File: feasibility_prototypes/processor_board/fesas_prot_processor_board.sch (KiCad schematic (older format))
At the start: 21 parts, among them P1 CONN_01X08, P10 CONN_01X02, P2 CONN_01X08, P3 CONN_01X02, P4 CONN_01X06, P5 CONN_01X08, P6 CONN_01X08, P7 CONN_01X08, P8 CONN_01X08, P9 CONN_01X02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

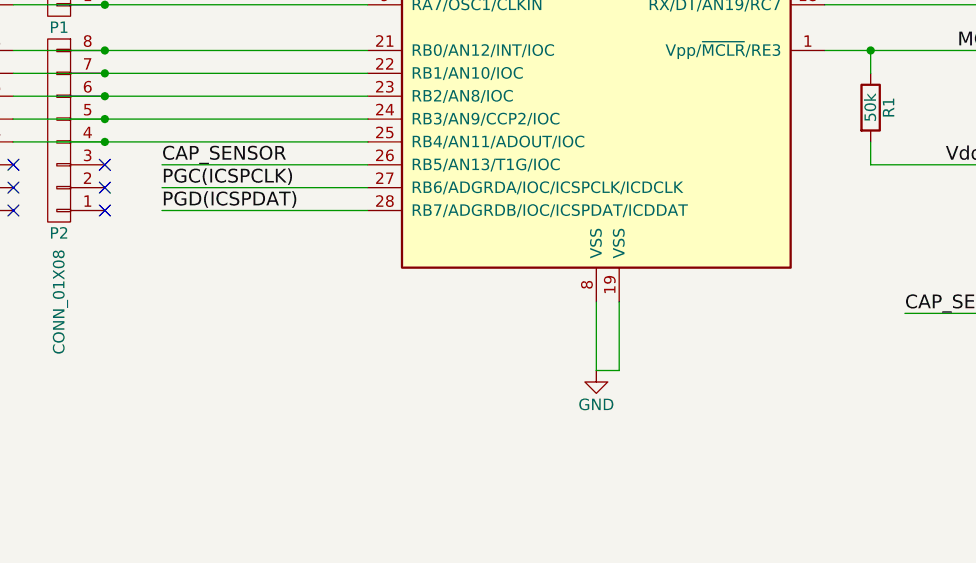
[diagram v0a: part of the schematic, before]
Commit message: Addded guard trace for cap-sense pad
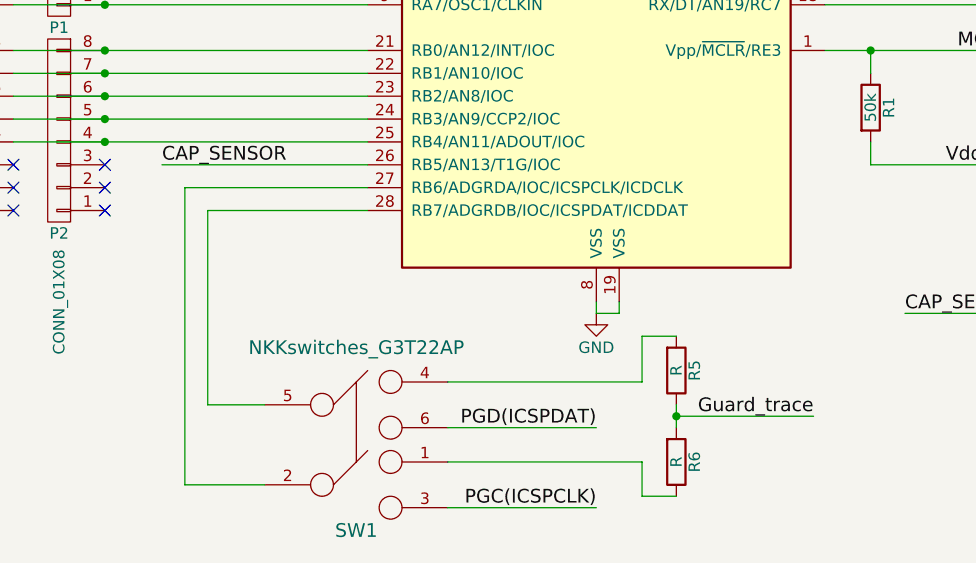
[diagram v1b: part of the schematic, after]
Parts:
- added R5, R6: R, Resistors_SMD:R_0805_HandSoldering, symbol R
- added SW1: NKKswitches_G3T22AP, med_conn_prototype_footprints:NKKSwitches_G3T22AP, symbol NKKswitches_G3T22AP
- P1, P2, P5: footprint Pin_Headers:Pin_Header_Straight_1x08_Pitch2.54mm -> med_conn_prototype_footprints:Sullins_SMD_pin_header_1x8_GBC36SABN-M30
- P10, P3, P9: footprint Pin_Headers:Pin_Header_Straight_1x02_Pitch2.54mm -> med_conn_prototype_footprints:Sullins_SMD_pin_header_1x2_GBC36SABN-M30
- P4: footprint Pin_Headers:Pin_Header_Straight_1x06_Pitch2.54mm -> med_conn_prototype_footprints:Sullins_SMD_pin_header_1x6_GBC36SABN-M30
- P6, P7, P8: footprint Pin_Headers:Pin_Header_Straight_1x08_Pitch2.54mm -> med_conn_prototype_footprints:wire_solder_pad_2.54mm_1x8
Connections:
- net PGC(ICSPCLK): now also SW1.3; no longer U1.27 (RB6/ADGRDA/IOC/ICSPCLK/ICDCLK)
- net PGD(ICSPDAT): now also SW1.6; no longer U1.28 (RB7/ADGRDB/IOC/ICSPDAT/ICDDAT)
- new net: SW1.2, U1.27 (RB6/ADGRDA/IOC/ICSPCLK/ICDCLK)
- new net: SW1.5, U1.28 (RB7/ADGRDB/IOC/ICSPDAT/ICDDAT)
- new net: R6.1, SW1.1
- new net: R5.2, SW1.4
- new net Guard_trace: R5.1, R6.2
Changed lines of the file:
@@
 F 0 "P4" H 8450 1400 50  0000 C CNN
 F 1 "CONN_01X06" V 8550 1050 50  0000 C CNN
-F 2 "Pin_Headers:Pin_Header_Straight_1x06_Pitch2.54mm" H 8450 1050 50  0001 C CNN
+F 2 "med_conn_prototype_footprints:Sullins_SMD_pin_header_1x6_GBC36SABN-M30" H 8450 1050 50  0001 C CNN
 F 3 "" H 8450 1050 50  0000 C CNN
 	1    8450 1050
@@
 F 0 "P3" H 6550 1200 50  0000 C CNN
 F 1 "CONN_01X02" V 6650 1050 50  0000 C CNN
-F 2 "Pin_Headers:Pin_Header_Straight_1x02_Pitch2.54mm" H 6550 1050 50  0001 C CNN
+F 2 "med_conn_prototype_footprints:Sullins_SMD_pin_header_1x2_GBC36SABN-M30" H 6550 1050 50  0001 C CNN
 F 3 "" H 6550 1050 50  0000 C CNN
 	1    6550 1050
@@
 Text Label 5900 3750 2    60   ~ 0
 MCLR/Vpp
-Text Label 2000 4450 0    60   ~ 0
-PGD(ICSPDAT)
-Text Label 2000 4350 0    60   ~ 0
+Text Label 3900 5750 2    60   ~ 0
 PGC(ICSPCLK)
 $Comp
@@
 F 0 "P1" H 1550 3650 50  0000 C CNN
 F 1 "CONN_01X08" V 1550 2500 50  0000 C CNN
-F 2 "Pin_Headers:Pin_Header_Straight_1x08_Pitch2.54mm" H 1550 3200 50  0001 C CNN
+F 2 "med_conn_prototype_footprints:Sullins_SMD_pin_header_1x8_GBC36SABN-M30" H 1550 3200 50  0001 C CNN
 F 3 "" H 1550 3200 50  0000 C CNN
 	1    1550 3200
@@
 F 0 "P2" H 1550 4550 50  0000 C CNN
 F 1 "CONN_01X08" V 1550 4850 50  0000 C CNN
-F 2 "Pin_Headers:Pin_Header_Straight_1x08_Pitch2.54mm" H 1550 4100 50  0001 C CNN
+F 2 "med_conn_prototype_footprints:Sullins_SMD_pin_header_1x8_GBC36SABN-M30" H 1550 4100 50  0001 C CNN
 F 3 "" H 1550 4100 50  0000 C CNN
 	1    1550 4100
@@
 F 0 "P5" H 6700 3650 50  0000 C CNN
 F 1 "CONN_01X08" V 6700 2550 50  0000 C CNN
-F 2 "Pin_Headers:Pin_Header_Straight_1x08_Pitch2.54mm" H 6700 3200 50  0001 C CNN
+F 2 "med_conn_prototype_footprints:Sullins_SMD_pin_header_1x8_GBC36SABN-M30" H 6700 3200 50  0001 C CNN
 F 3 "" H 6700 3200 50  0000 C CNN
 	1    6700 3200
@@
 F 0 "P8" H 7100 3650 50  0000 C CNN
 F 1 "CONN_01X08" V 7100 2550 50  0000 C CNN
-F 2 "Pin_Headers:Pin_Header_Straight_1x08_Pitch2.54mm" H 7100 3200 50  0001 C CNN
+F 2 "med_conn_prototype_footprints:wire_solder_pad_2.54mm_1x8" H 7100 3200 50  0001 C CNN
 F 3 "" H 7100 3200 50  0000 C CNN
 	1    7100 3200
@@
 F 0 "P6" H 1150 3650 50  0000 C CNN
 F 1 "CONN_01X08" V 1150 2500 50  0000 C CNN
-F 2 "Pin_Headers:Pin_Header_Straight_1x08_Pitch2.54mm" H 1150 3200 50  0001 C CNN
+F 2 "med_conn_prototype_footprints:wire_solder_pad_2.54mm_1x8" H 1150 3200 50  0001 C CNN
 F 3 "" H 1150 3200 50  0000 C CNN
 	1    1150 3200
@@
 F 0 "P7" H 1150 4550 50  0000 C CNN
 F 1 "CONN_01X08" V 1150 4850 50  0000 C CNN
-F 2 "Pin_Headers:Pin_Header_Straight_1x08_Pitch2.54mm" H 1150 4100 50  0001 C CNN
+F 2 "med_conn_prototype_footprints:wire_solder_pad_2.54mm_1x8" H 1150 4100 50  0001 C CNN
 F 3 "" H 1150 4100 50  0000 C CNN
 	1    1150 4100
@@
 L GND #PWR05
 U 1 1 58A597DF
-P 3900 5150
-F 0 "#PWR05" H 3900 4900 50  0001 C CNN
-F 1 "GND" H 3900 5000 50  0000 C CNN
-F 2 "" H 3900 5150 50  0000 C CNN
-F 3 "" H 3900 5150 50  0000 C CNN
-	1    3900 5150
+P 3900 4900
+F 0 "#PWR05" H 3900 4650 50  0001 C CNN
+F 1 "GND" H 3900 4750 50  0000 C CNN
+F 2 "" H 3900 4900 50  0000 C CNN
+F 3 "" H 3900 4900 50  0000 C CNN
+	1    3900 4900
 	1    0    0    -1
 $EndComp
@@
 F 0 "P9" H 6950 1500 50  0000 C CNN
 F 1 "CONN_01X02" V 7050 1650 50  0000 C CNN
-F 2 "Pin_Headers:Pin_Header_Straight_1x02_Pitch2.54mm" H 6950 1650 50  0001 C CNN
+F 2 "med_conn_prototype_footprints:Sullins_SMD_pin_header_1x2_GBC36SABN-M30" H 6950 1650 50  0001 C CNN
 F 3 "" H 6950 1650 50  0000 C CNN
 	1    6950 1650
@@
 F 0 "P10" H 7350 1800 50  0000 C CNN
 F 1 "CONN_01X02" V 7450 1650 50  0000 C CNN
-F 2 "Pin_Headers:Pin_Header_Straight_1x02_Pitch2.54mm" H 7350 1650 50  0001 C CNN
+F 2 "med_conn_prototype_footprints:Sullins_SMD_pin_header_1x2_GBC36SABN-M30" H 7350 1650 50  0001 C CNN
 F 3 "" H 7350 1650 50  0000 C CNN
 	1    7350 1650
@@
 	4900 3750 5900 3750
 Wire Wire Line
-	2000 4350 2900 4350
-Wire Wire Line
-	2900 4450 2000 4450
-Wire Wire Line
 	3900 2450 3900 1850
-Wire Wire Line
-	3900 4850 3900 5150
-Wire Wire Line
-	3900 5150 4000 5150
-Wire Wire Line
-	4000 5150 4000 4850
 Wire Wire Line
 	6600 1250 6600 1350
@@
 NoConn ~ 5600 2350
 NoConn ~ 5100 2350
+Wire Wire Line
+	3900 4900 3900 4850
+Wire Wire Line
+	3900 4900 4000 4900
+Wire Wire Line
+	4000 4900 4000 4850
+Wire Wire Line
+	2900 4450 2200 4450
+Wire Wire Line
+	2200 4450 2200 5300
+Wire Wire Line
+	2200 5300 2450 5300
+Wire Wire Line
+	2900 4350 2100 4350
+Wire Wire Line
+	2100 4350 2100 5650
+Wire Wire Line
+	2100 5650 2450 5650
+Wire Wire Line
+	3250 5400 3900 5400
+Wire Wire Line
+	3250 5750 3900 5750
+$Comp
+L NKKswitches_G3T22AP SW1
+U 1 1 58AD9EC0
+P 2850 5050
+F 0 "SW1" H 2850 4250 60  0000 C CNN
+F 1 "NKKswitches_G3T22AP" H 2850 5050 60  0000 C CNN
+F 2 "med_conn_prototype_footprints:NKKSwitches_G3T22AP" H 2850 5050 60  0001 C CNN
+F 3 "" H 2850 5050 60  0001 C CNN
+	1    2850 5050
+	1    0    0    -1
+$EndComp
+$Comp
+L R R6
+U 1 1 58ADA5F0
+P 4250 5550
+F 0 "R6" V 4330 5550 50  0000 C CNN
+F 1 "R" V 4250 5550 50  0000 C CNN
+F 2 "Resistors_SMD:R_0805_HandSoldering" V 4180 5550 50  0001 C CNN
+F 3 "" H 4250 5550 50  0000 C CNN
+	1    4250 5550
+	1    0    0    1
+$EndComp
+Text Label 3900 5400 2    60   ~ 0
+PGD(ICSPDAT)
+$Comp
+L R R5
+U 1 1 58ADB679
+P 4250 5150
+F 0 "R5" V 4330 5150 50  0000 C CNN
+F 1 "R" V 4250 5150 50  0000 C CNN
+F 2 "Resistors_SMD:R_0805_HandSoldering" V 4180 5150 50  0001 C CNN
+F 3 "" H 4250 5150 50  0000 C CNN
+	1    4250 5150
+	1    0    0    1
+$EndComp
+Wire Wire Line
+	3250 5200 4100 5200
+Wire Wire Line
+	4100 5200 4100 5000
+Wire Wire Line
+	4100 5000 4250 5000
+Wire Wire Line
+	3250 5550 4100 5550
+Wire Wire Line
+	4100 5550 4100 5700
+Wire Wire Line
+	4100 5700 4250 5700
+Wire Wire Line
+	4250 5400 4250 5300
+Wire Wire Line
+	4250 5350 4850 5350
+Connection ~ 4250 5350
+Text Label 4850 5350 2    60   ~ 0
+Guard_trace
 $EndSCHEMATC

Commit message: Added RJ11 connector to processor board, finished IR board.
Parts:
- U1: footprint Housings_SOIC:SOIC-28W_7.5x17.9mm_Pitch1.27mm -> med_conn_prototype_footprints:SOIC-28W_7.5x17.9mm_Pitch1.27mm
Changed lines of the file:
@@
 F 0 "U1" H 4100 4850 50  0000 L CNN
 F 1 "PIC16(L)F1512-I/SO" H 4100 4750 50  0000 L CNN
-F 2 "Housings_SOIC:SOIC-28W_7.5x17.9mm_Pitch1.27mm" H 3900 3650 50  0001 C CNN
+F 2 "med_conn_prototype_footprints:SOIC-28W_7.5x17.9mm_Pitch1.27mm" H 3900 3650 50  0001 C CNN
 F 3 "" H 3900 3650 50  0000 C CNN
 	1    3900 3650
